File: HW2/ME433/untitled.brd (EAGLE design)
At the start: 50 x 50 mm, 19 parts, among them SW1 DIP-SLIDE-SWITCH(3P-11.6X4.0X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

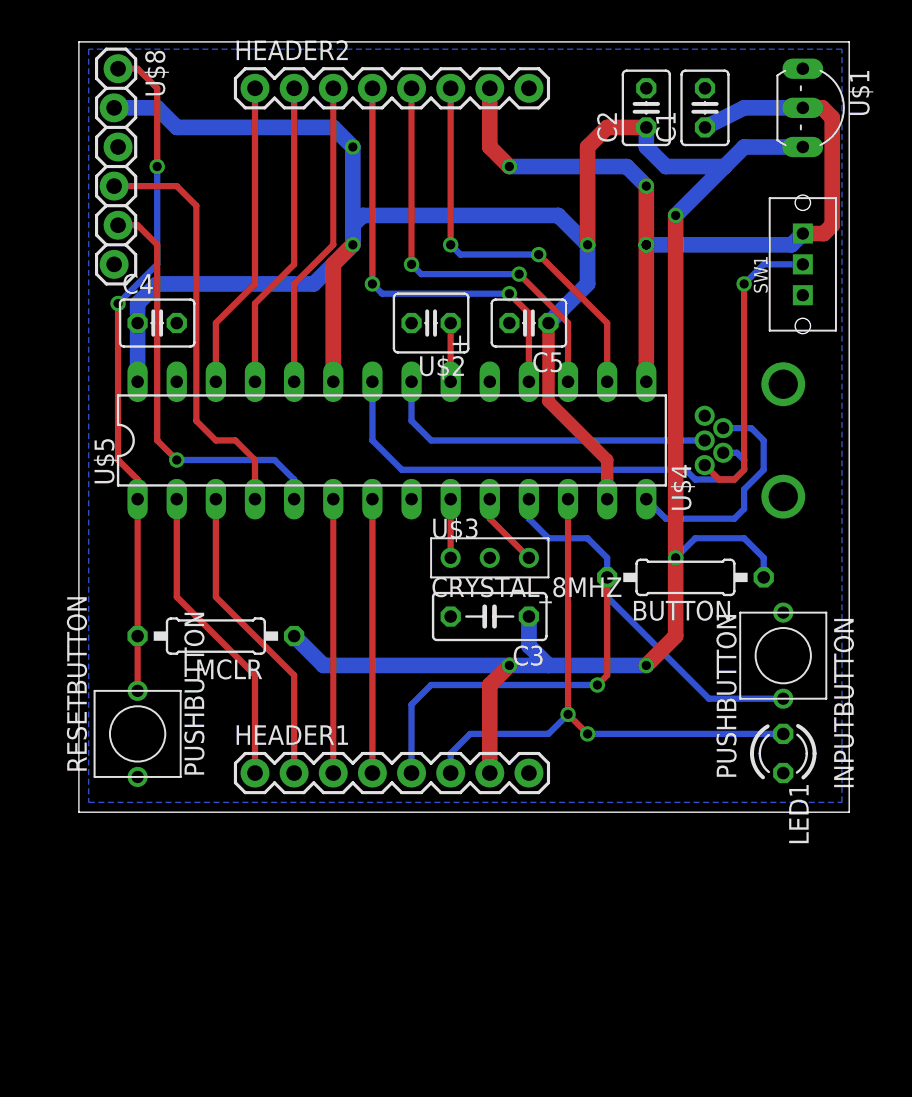
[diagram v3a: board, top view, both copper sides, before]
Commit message: board spacing revision
got rid of most clearance errors, resized buttons and resonator pin
width
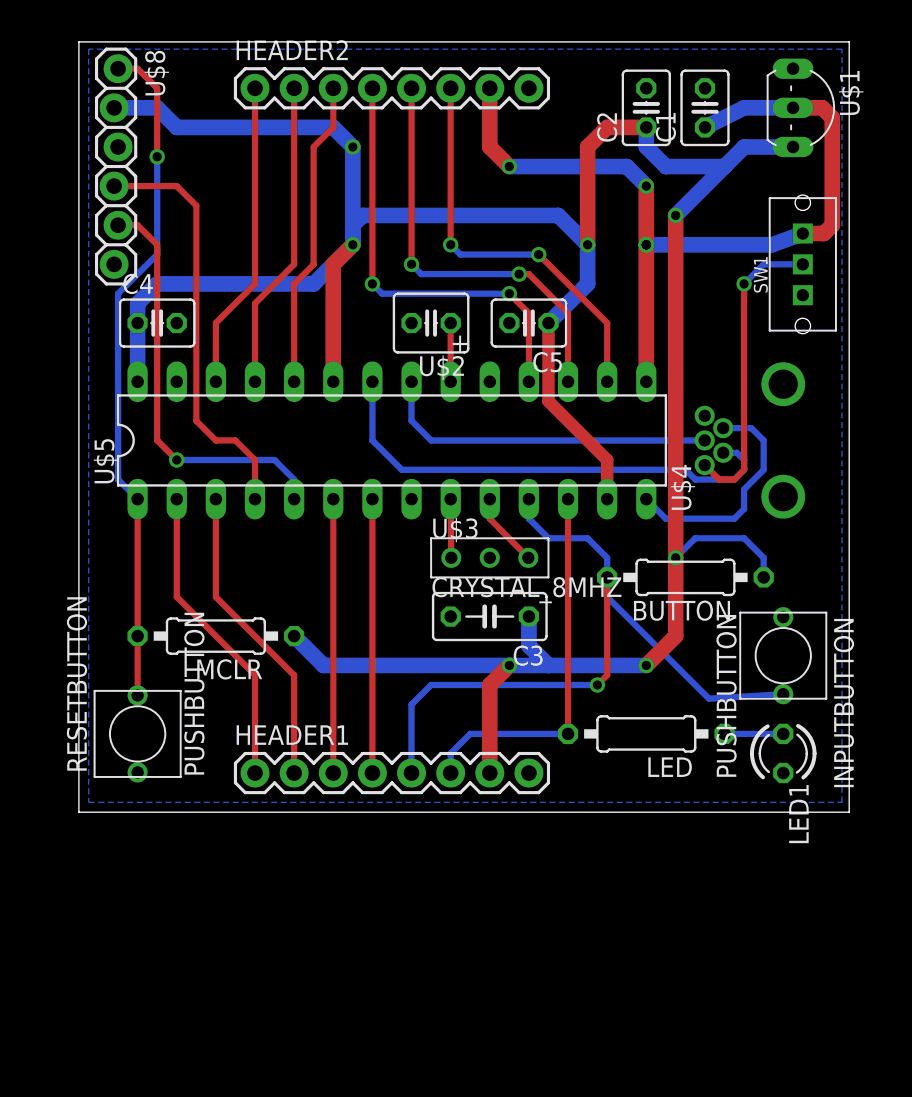
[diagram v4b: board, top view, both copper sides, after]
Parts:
- added LED: 330, components:0207/10
- moved U$1 0.63 mm to (47.6, 45.7)
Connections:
- new net N$1: LED.1, LED1.A
- net A4: now also LED.2; no longer LED1.A
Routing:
- net A4: track 38.4 -> 24.7 mm, vias 2 -> 0
- net N$1: track 0.00 -> 3.81 mm
- net +3V3: track 194.0 -> 193.4 mm
- net MCLR: track 43.8 -> 44.1 mm, vias 2 -> 1
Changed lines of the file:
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@@
 <element name="BUTTON" library="components" package="0207/10" value="10k" x="39.37" y="15.24" rot="R180"/>
 <element name="MCLR" library="components" package="0207/10" value="10k" x="8.89" y="11.43" rot="R180"/>
-<element name="U$1" library="components" package="TO92-EBC" value="VOLTAGE_REGULATOR_MCP1702" x="48.26" y="45.72" rot="R270"/>
+<element name="U$1" library="components" package="TO92-EBC" value="VOLTAGE_REGULATOR_MCP1702" x="47.625" y="45.72" rot="R270"/>
 <element name="U$2" library="components" package="C025-040X050POL" value="CAP_TANT_10UFSHORT" x="22.86" y="31.75" rot="R180"/>
 <element name="U$3" library="components" package="CRYSTAL_8MHZ" value="CRYSTAL_8MHZ" x="26.67" y="16.51"/>
@@
 <attribute name="PROD_ID" value="CONN-08437" x="11.43" y="46.99" size="1.778" layer="27" display="off"/>
 </element>
+<element name="LED" library="components" package="0207/10" value="330" x="36.83" y="5.08" rot="R180"/>
 </elements>
 <signals>
@@
 <wire x1="36.83" y1="43.18" x2="38.1" y2="41.91" width="1.016" layer="16"/>
 <wire x1="38.1" y1="41.91" x2="41.91" y2="41.91" width="1.016" layer="16"/>
-<wire x1="46.99" y1="43.18" x2="43.18" y2="43.18" width="1.016" layer="16"/>
+<wire x1="46.355" y1="43.18" x2="43.18" y2="43.18" width="1.016" layer="16"/>
 <wire x1="43.18" y1="43.18" x2="41.91" y2="41.91" width="1.016" layer="16"/>
 <wire x1="17.78" y1="36.83" x2="15.24" y2="34.29" width="1.016" layer="16"/>
@@
 <contactref element="SW1" pad="RIGHT"/>
 <contactref element="HEADER2" pad="7"/>
-<wire x1="46.99" y1="37.56" x2="46.26" y2="36.83" width="1.016" layer="16"/>
+<wire x1="46.99" y1="37.56" x2="44.99" y2="36.83" width="1.016" layer="16"/>
 <wire x1="48.355" y1="37.56" x2="46.99" y2="37.56" width="1.016" layer="1"/>
 <wire x1="40.64" y1="44.45" x2="43.18" y2="45.72" width="1.016" layer="16"/>
-<wire x1="43.18" y1="45.72" x2="46.99" y2="45.72" width="1.016" layer="16"/>
-<wire x1="36.83" y1="36.83" x2="46.26" y2="36.83" width="1.016" layer="16"/>
+<wire x1="43.18" y1="45.72" x2="46.355" y2="45.72" width="1.016" layer="16"/>
+<wire x1="36.83" y1="36.83" x2="44.99" y2="36.83" width="1.016" layer="16"/>
 <wire x1="48.355" y1="37.56" x2="48.895" y2="38.1" width="1.016" layer="1"/>
 <wire x1="48.895" y1="38.1" x2="48.895" y2="45.085" width="1.016" layer="1"/>
 <wire x1="48.895" y1="45.085" x2="48.26" y2="45.72" width="1.016" layer="1"/>
-<wire x1="48.26" y1="45.72" x2="46.99" y2="45.72" width="1.016" layer="1"/>
+<wire x1="48.26" y1="45.72" x2="46.355" y2="45.72" width="1.016" layer="1"/>
 <wire x1="36.83" y1="27.94" x2="36.83" y2="36.83" width="1.016" layer="1"/>
 <via x="36.83" y="36.83" extent="1-16" drill="0.6"/>
@@
 <contactref element="MCLR" pad="2"/>
 <contactref element="RESETBUTTON" pad="P$2"/>
-<wire x1="5.08" y1="35.56" x2="2.54" y2="33.02" width="0.4064" layer="16"/>
-<via x="2.54" y="33.02" extent="1-16" drill="0.6"/>
-<wire x1="2.54" y1="33.02" x2="2.54" y2="22.86" width="0.4064" layer="1"/>
-<wire x1="2.54" y1="22.86" x2="3.81" y2="21.59" width="0.4064" layer="1"/>
-<wire x1="3.81" y1="21.59" x2="3.81" y2="20.32" width="0.4064" layer="1"/>
 <wire x1="3.81" y1="20.32" x2="3.81" y2="11.43" width="0.4064" layer="1"/>
-<wire x1="3.81" y1="7.874" x2="3.81" y2="11.43" width="0.4064" layer="1"/>
+<wire x1="3.81" y1="7.58" x2="3.81" y2="11.43" width="0.4064" layer="1"/>
 <wire x1="2.54" y1="48.26" x2="3.81" y2="48.26" width="0.4064" layer="1"/>
 <wire x1="3.81" y1="48.26" x2="5.08" y2="46.99" width="0.4064" layer="1"/>
-<wire x1="5.08" y1="46.99" x2="5.08" y2="41.91" width="0.4064" layer="1"/>
-<via x="5.08" y="41.91" extent="1-16" drill="0.6"/>
-<wire x1="5.08" y1="41.91" x2="5.08" y2="35.56" width="0.4064" layer="16"/>
+<wire x1="5.08" y1="46.99" x2="5.08" y2="42.545" width="0.4064" layer="1"/>
+<via x="5.08" y="42.545" extent="1-16" drill="0.6"/>
+<wire x1="5.08" y1="42.545" x2="5.08" y2="36.195" width="0.4064" layer="16"/>
+<wire x1="5.08" y1="36.195" x2="2.54" y2="33.655" width="0.4064" layer="16"/>
+<wire x1="2.54" y1="33.655" x2="2.54" y2="21.59" width="0.4064" layer="16"/>
+<wire x1="2.54" y1="21.59" x2="3.81" y2="20.32" width="0.4064" layer="16"/>
 </signal>
 <signal name="PICKITD">
@@
 <contactref element="U$5" pad="9"/>
 <contactref element="U$3" pad="OSC1"/>
-<wire x1="24.13" y1="20.32" x2="24.13" y2="16.51" width="0.4064" layer="1"/>
+<wire x1="24.13" y1="20.32" x2="24.17" y2="16.51" width="0.4064" layer="1"/>
 </signal>
 <signal name="OSC2">
@@
 <contactref element="U$3" pad="OSC2"/>
 <wire x1="26.67" y1="20.32" x2="26.67" y2="19.05" width="0.4064" layer="1"/>
-<wire x1="26.67" y1="19.05" x2="29.21" y2="16.51" width="0.4064" layer="1"/>
+<wire x1="26.67" y1="19.05" x2="29.17" y2="16.51" width="0.4064" layer="1"/>
 </signal>
 <signal name="VCAP">
@@
 <wire x1="33.02" y1="17.78" x2="34.29" y2="16.51" width="0.4064" layer="16"/>
 <wire x1="34.29" y1="16.51" x2="34.29" y2="15.24" width="0.4064" layer="16"/>
-<wire x1="45.72" y1="7.366" x2="40.894" y2="7.366" width="0.4064" layer="16"/>
+<wire x1="45.72" y1="7.66" x2="40.894" y2="7.366" width="0.4064" layer="16"/>
 <wire x1="40.894" y1="7.366" x2="34.29" y2="13.97" width="0.4064" layer="16"/>
 <wire x1="21.59" y1="6.985" x2="21.59" y2="2.54" width="0.4064" layer="16"/>
@@
 <signal name="A4">
 <contactref element="HEADER1" pad="6"/>
-<contactref element="LED1" pad="A"/>
 <contactref element="U$5" pad="12"/>
-<wire x1="31.75" y1="20.32" x2="31.75" y2="6.35" width="0.4064" layer="1"/>
-<wire x1="31.75" y1="6.35" x2="33.02" y2="5.08" width="0.4064" layer="1"/>
-<via x="33.02" y="5.08" extent="1-16" drill="0.6"/>
-<wire x1="33.02" y1="5.08" x2="45.72" y2="5.08" width="0.4064" layer="16"/>
-<via x="31.75" y="6.35" extent="1-16" drill="0.6"/>
-<wire x1="31.75" y1="6.35" x2="30.48" y2="5.08" width="0.4064" layer="16"/>
-<wire x1="30.48" y1="5.08" x2="25.4" y2="5.08" width="0.4064" layer="16"/>
+<contactref element="LED" pad="2"/>
+<wire x1="31.75" y1="20.32" x2="31.75" y2="5.08" width="0.4064" layer="1"/>
+<wire x1="31.75" y1="5.08" x2="25.4" y2="5.08" width="0.4064" layer="16"/>
 <wire x1="25.4" y1="5.08" x2="24.13" y2="3.81" width="0.4064" layer="16"/>
 <wire x1="24.13" y1="3.81" x2="24.13" y2="2.54" width="0.4064" layer="16"/>
@@
 <contactref element="HEADER2" pad="3"/>
 <wire x1="13.97" y1="27.94" x2="13.97" y2="34.29" width="0.4064" layer="1"/>
-<wire x1="13.97" y1="34.29" x2="16.51" y2="36.83" width="0.4064" layer="1"/>
-<wire x1="16.51" y1="36.83" x2="16.51" y2="46.99" width="0.4064" layer="1"/>
+<wire x1="13.97" y1="34.29" x2="15.24" y2="35.56" width="0.4064" layer="1"/>
+<wire x1="15.24" y1="35.56" x2="15.24" y2="43.18" width="0.4064" layer="1"/>
+<wire x1="15.24" y1="43.18" x2="16.51" y2="44.45" width="0.4064" layer="1"/>
+<wire x1="16.51" y1="44.45" x2="16.51" y2="46.99" width="0.4064" layer="1"/>
 </signal>
 <signal name="B9">
@@
 <contactref element="U$5" pad="17"/>
 <contactref element="HEADER2" pad="5"/>
-<wire x1="31.75" y1="27.94" x2="31.75" y2="31.75" width="0.4064" layer="1"/>
-<wire x1="31.75" y1="31.75" x2="28.575" y2="34.925" width="0.4064" layer="1"/>
 <via x="28.575" y="34.925" extent="1-16" drill="0.6"/>
 <wire x1="28.575" y1="34.925" x2="22.225" y2="34.925" width="0.4064" layer="16"/>
@@
 <via x="21.59" y="35.56" extent="1-16" drill="0.6"/>
 <wire x1="21.59" y1="35.56" x2="21.59" y2="46.99" width="0.4064" layer="1"/>
+<wire x1="31.75" y1="27.94" x2="31.75" y2="32.385" width="0.4064" layer="1"/>
+<wire x1="31.75" y1="32.385" x2="29.21" y2="34.925" width="0.4064" layer="1"/>
+<wire x1="29.21" y1="34.925" x2="28.575" y2="34.925" width="0.4064" layer="1"/>
 </signal>
 <signal name="B7">
@@
 <wire x1="24.13" y1="36.83" x2="24.13" y2="46.99" width="0.4064" layer="1"/>
 </signal>
+<signal name="N$1">
+<contactref element="LED1" pad="A"/>
+<contactref element="LED" pad="1"/>
+<wire x1="41.91" y1="5.08" x2="45.72" y2="5.08" width="0.4064" layer="16"/>
+</signal>
 </signals>

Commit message: presmash
layout complete, presmash and prenaming
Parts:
- added PWR: (no value), components:LED3MM
- added RPWR: 330, components:0207/10
- moved C3 9.25 mm to (17.8, 15.2), turned to 0 degrees
- moved U$3 1.27 mm to (26.7, 15.2)
- moved C4 1.27 mm to (5.08, 30.5)
- moved C5 1.27 mm to (29.2, 30.5)
- moved U$2 1.27 mm to (22.9, 30.5)
- moved U$5 1.27 mm to (20.3, 22.9)
- moved U$8 1.27 mm to (2.54, 47.0)
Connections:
- new net N$2: PWR.K, RPWR.1
- net +3V3: now also PWR.A
- net GND: now also RPWR.2
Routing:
- net B4: track 48.4 -> 45.3 mm
- net MCLR: track 44.1 -> 42.6 mm
- net A4: track 24.7 -> 23.4 mm
- net USBD-: track 31.4 -> 30.2 mm
- net USBD+: track 22.1 -> 20.8 mm
- net B9: track 28.1 -> 29.4 mm
- net B8: track 27.4 -> 28.6 mm
- net B7: track 26.2 -> 27.5 mm
- net B3: track 17.8 -> 16.5 mm
- net B2: track 17.8 -> 16.5 mm
- net B15: track 20.1 -> 21.4 mm
- net B13: track 20.1 -> 21.4 mm
- net A1: track 19.9 -> 18.6 mm
- net B14: track 20.1 -> 21.4 mm
- net A0: track 19.9 -> 18.6 mm
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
